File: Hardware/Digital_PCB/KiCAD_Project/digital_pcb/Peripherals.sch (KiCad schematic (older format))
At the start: 13 parts, among them U2 BME280, U3 BNO055, Y2 32.768kHz

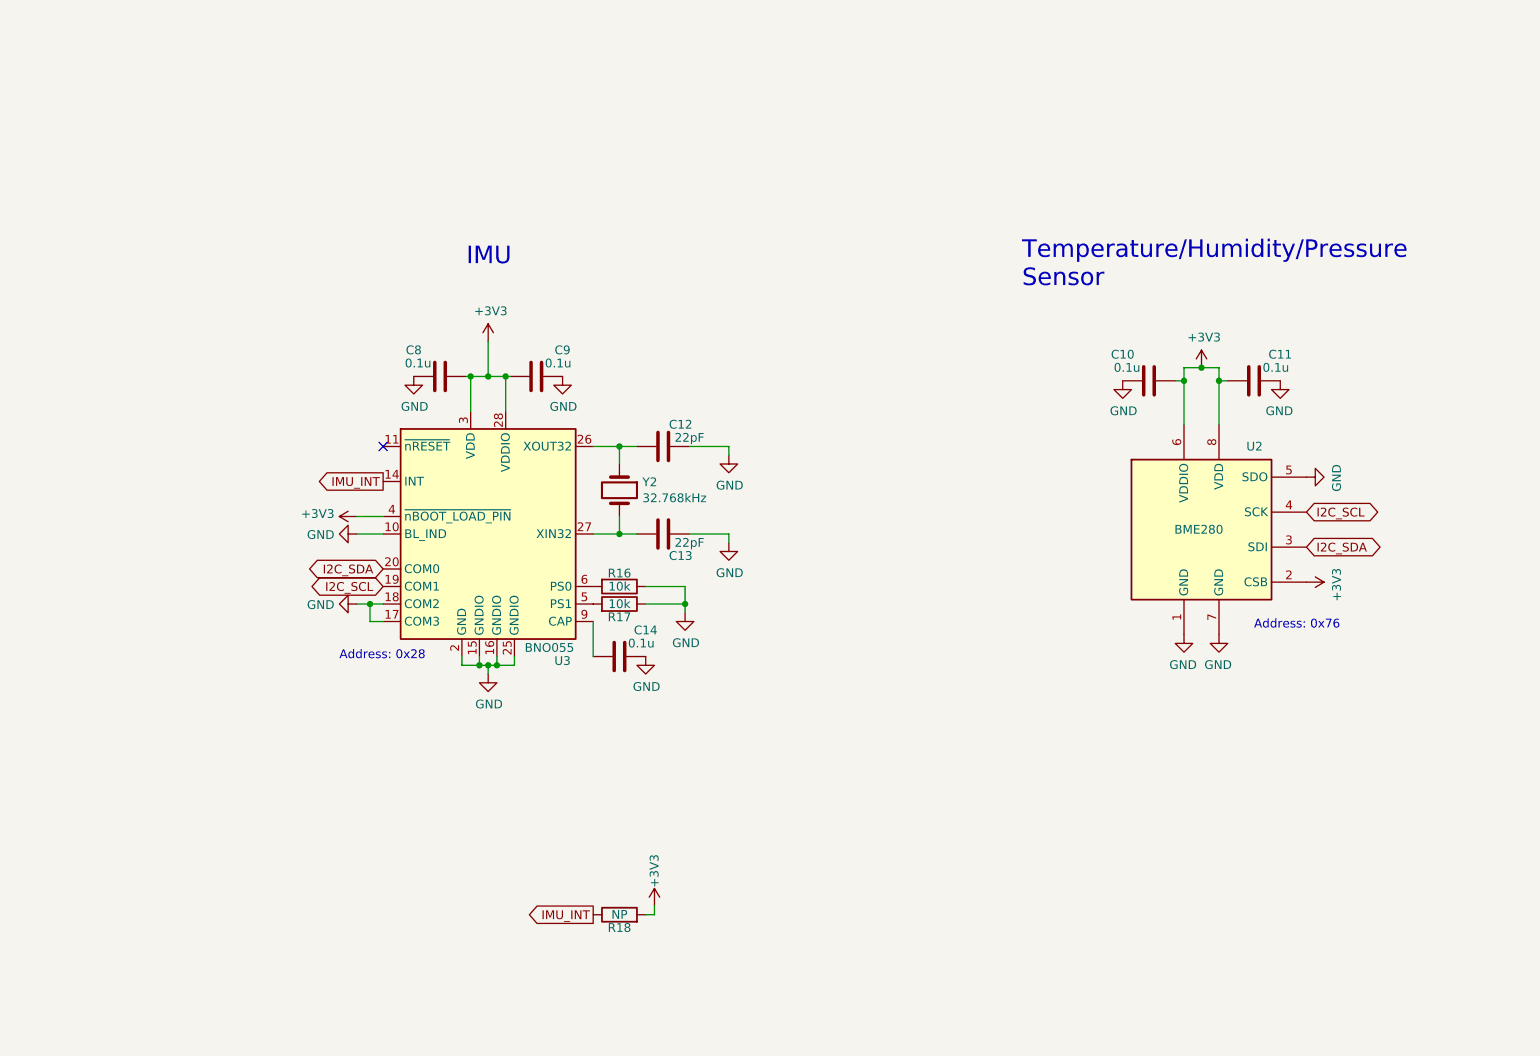
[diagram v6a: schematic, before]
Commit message: Add activity LED and another IMU footprint. Closes #49 #45
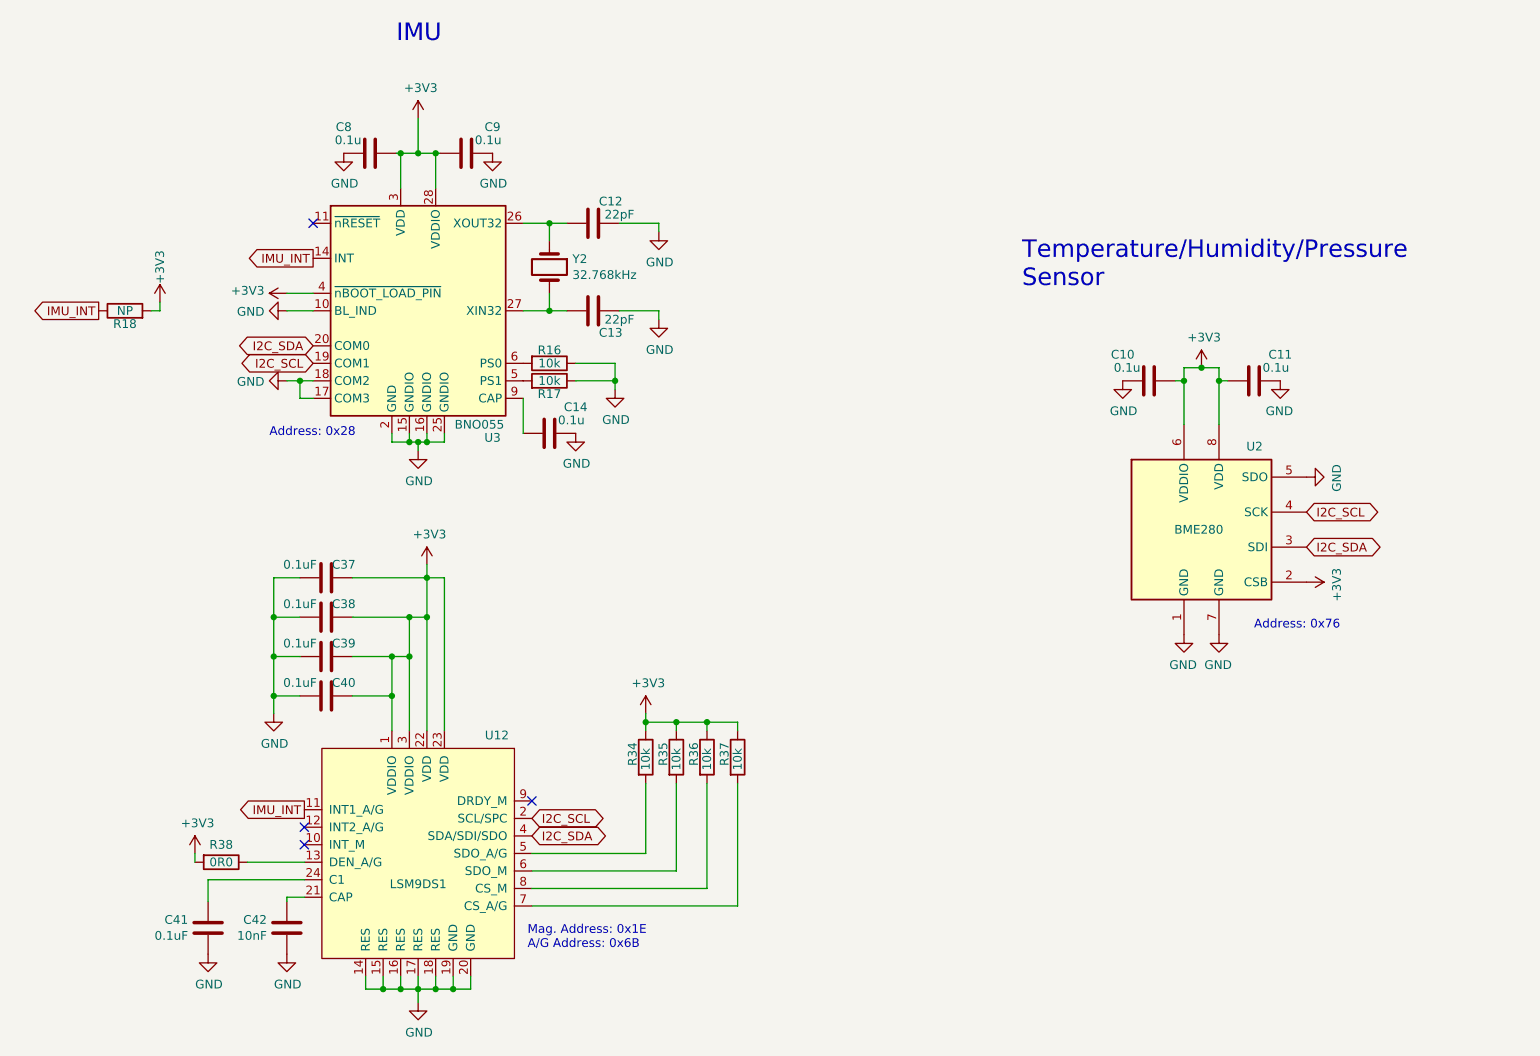
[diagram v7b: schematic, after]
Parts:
- added C37, C38, C39, C40, C41: 1-0000007, capacitors_0603:1-0000007, symbol capacitors_0603:1-0000007
- added C42: 1-0000014, capacitors_0603:1-0000014, symbol capacitors_0603:1-0000014
- added R34, R35, R36, R37: 1-0000010, resistors_0603:1-0000010, symbol resistors_0603:1-0000010
- added R38: 1-0000006, resistors_0603:1-0000006, symbol resistors_0603:1-0000006
- added U12: 1-0000925, sensors:1-0000925, symbol sensors:1-0000925
- C12, C13, C14, R16, R17, U3, Y2: Populated 1 -> 0
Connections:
- net +3V3: now also C37.2, C38.2, C39.2, C40.2, R34.1, R35.1, R36.1, R37.1, R38.2, U12.1 (VDDIO), U12.22 (VDD), U12.23 (VDD), U12.3 (VDDIO)
- net GND: now also C37.1, C38.1, C39.1, C40.1, C41.1, C42.1, U12.14 (RES), U12.15 (RES), U12.16 (RES), U12.17 (RES), U12.18 (RES), U12.19 (GND), U12.20 (GND)
- net I2C_SCL: now also U12.2 (SCL/SPC)
- net I2C_SDA: now also U12.4 (SDA/SDI/SDO)
- net IMU_INT: now also U12.11 (INT1_A/G)
- new net: R38.1, U12.13 (DEN_A/G)
- new net: C42.2, U12.21 (CAP)
- new net: C41.2, U12.24 (C1)
- new net: R34.2, U12.5 (SDO_A/G)
- new net: R35.2, U12.6 (SDO_M)
- new net: R37.2, U12.7 (CS_A/G)
- new net: R36.2, U12.8 (CS_M)
- no-connect marks 1 -> 4
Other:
- note added: "Mag. Address: 0x1E\nA/G Address: 0x6B"
- moved on the sheet: C12, C13, C14, C8, C9, R16, R17, R18, U3, Y2
